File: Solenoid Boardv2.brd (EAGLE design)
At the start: 100 x 80 mm, 38 parts, among them Y2 ECS-80-S-4X

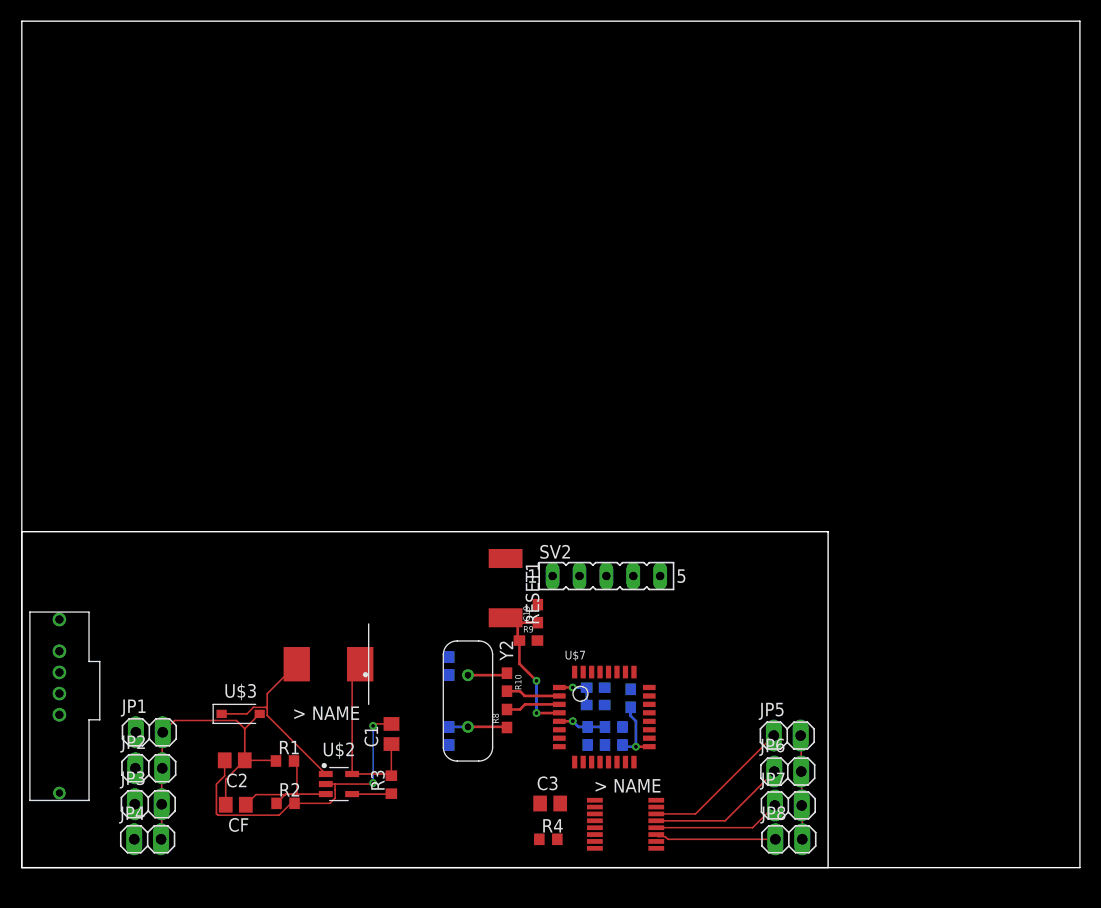
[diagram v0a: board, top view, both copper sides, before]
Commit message: Made progress on V2, added polygons and headers for step down converter
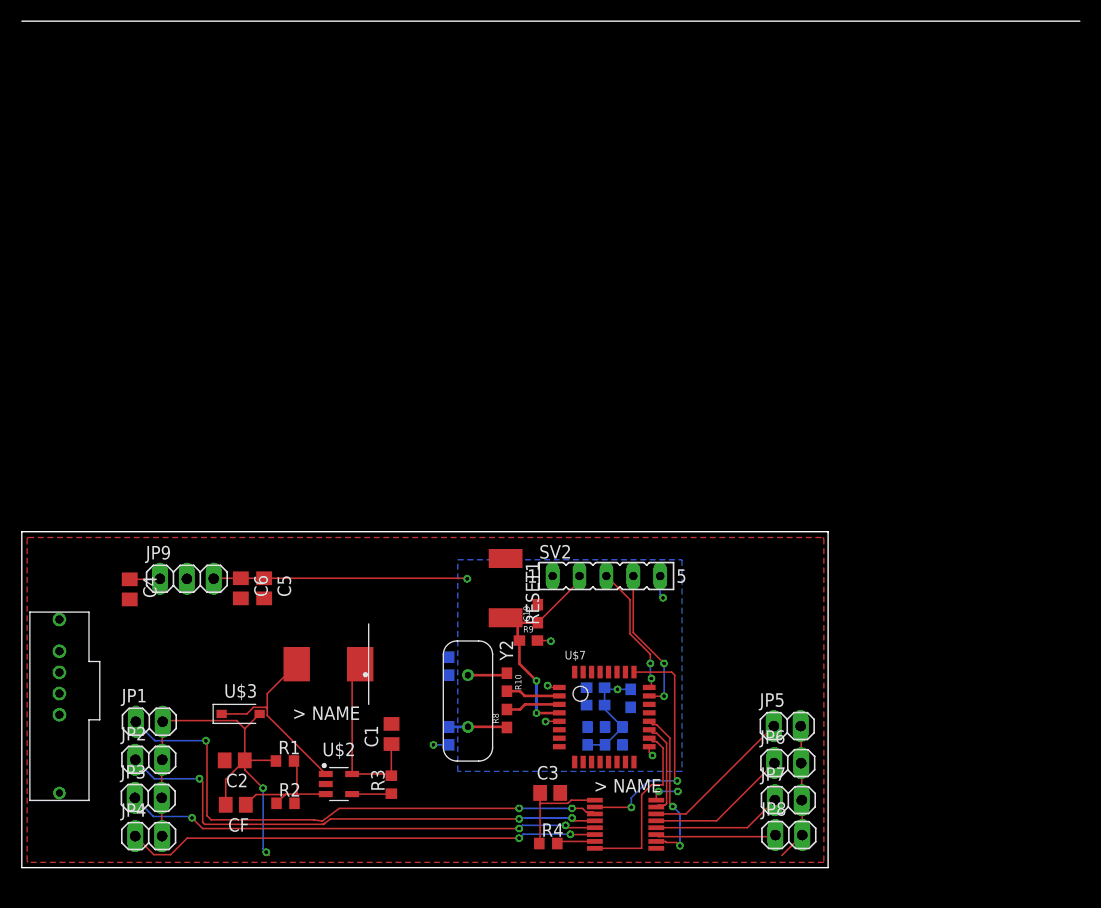
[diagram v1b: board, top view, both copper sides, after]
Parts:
- added C4: 10 µF, rcl:C0805
- added C5, C6: 47 µF, rcl:C0805
- added JP9: (no value), pinhead:1X03
- moved C3 1.00 mm to (49.9, 7.06)
- moved JP1 1.00 mm to (12.1, 13.8)
- moved JP5 0.90 mm to (72.3, 13.4)
- moved JP6 0.80 mm to (72.4, 9.88)
- moved JP2 0.80 mm to (12.0, 10.2)
- moved JP3 0.60 mm to (11.9, 6.59)
- moved JP7 0.50 mm to (72.4, 6.38)
- moved R4 0.40 mm to (49.8, 2.28)
- moved JP8 0.40 mm to (72.5, 3.08)
- moved JP4 0.32 mm to (12.0, 2.98)
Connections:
- net +12V: now also C4.1, JP9.1
- net +3V3: now also C5.1, C6.1, JP9.3
- net GND: now also C4.2, C5.2, C6.2, JP9.2
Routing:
- net DRAIN0: track 0.00 -> 51.9 mm, vias 0 -> 3
- net DRAIN1: track 0.00 -> 48.5 mm, vias 0 -> 3
- net DRAIN3: track 0.00 -> 45.0 mm, vias 0 -> 2
- net DRAIN2: track 0.00 -> 44.9 mm, vias 0 -> 3
- net SER_IN: track 0.00 -> 23.4 mm, vias 0 -> 2
- net G: track 0.00 -> 17.1 mm
- net +3V3: track 15.3 -> 30.9 mm, vias 3 -> 6
- net RCK: track 0.00 -> 15.6 mm, vias 0 -> 2
- net GND: track 30.4 -> 15.3 mm, vias 2 -> 4
- net SWDIO: track 0.00 -> 14.0 mm, vias 0 -> 2
- net +24V: track 41.5 -> 54.9 mm, vias 0 -> 2
- net SWCLK: track 0.00 -> 12.4 mm, vias 0 -> 2
- net +3.3V: track 0.00 -> 10.1 mm
- net SRCK: track 0.00 -> 8.99 mm
- net NRST: track 14.7 -> 20.7 mm
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- added copper zone on layer 16, net +3V3
- added copper zone on layer 1, net GND
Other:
- board size 100 x 80 mm -> 76.2 x 31.8 mm

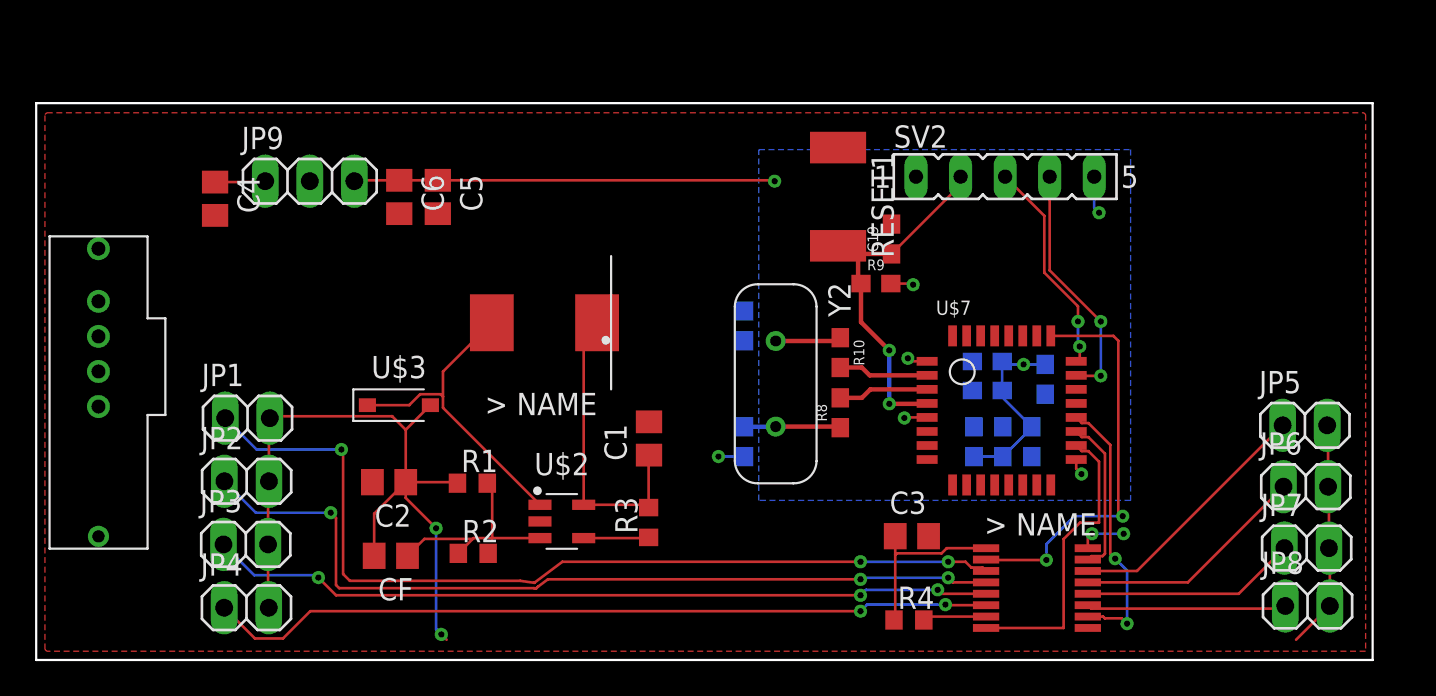
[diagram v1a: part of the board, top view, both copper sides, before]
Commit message: Added the can module
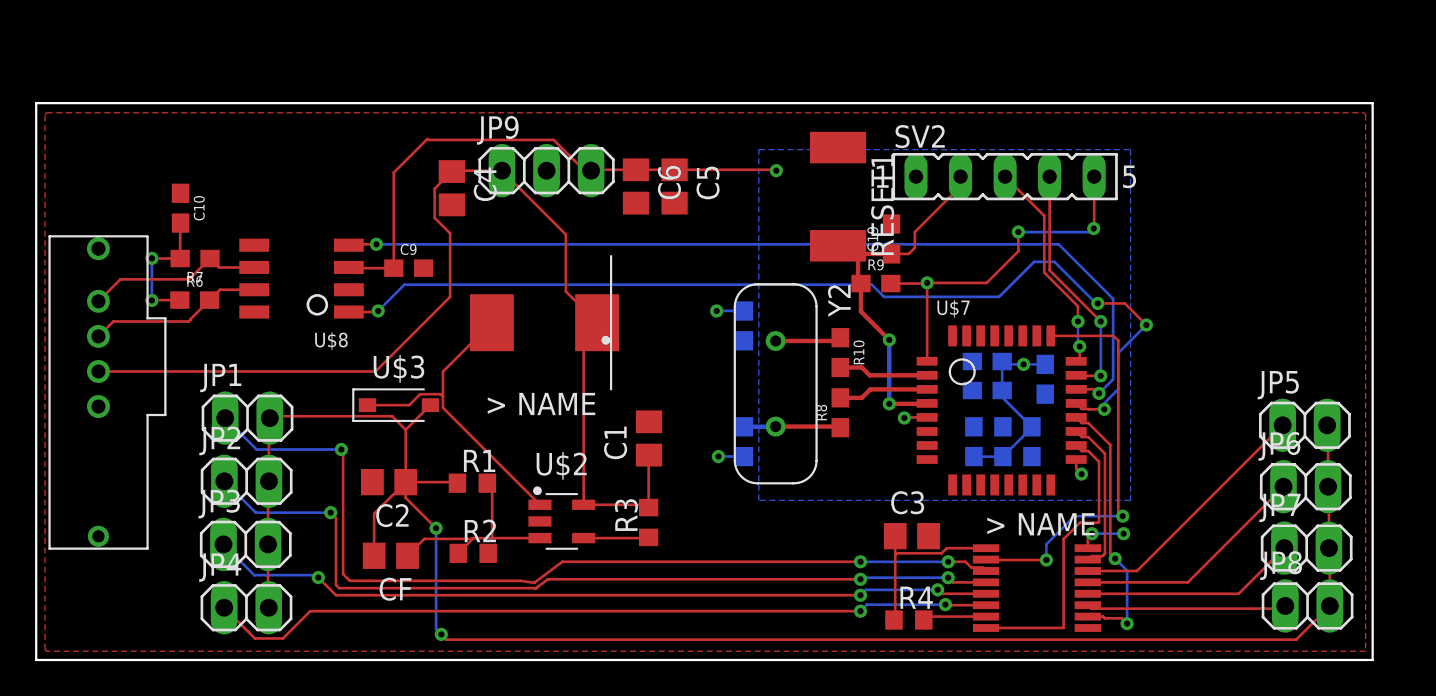
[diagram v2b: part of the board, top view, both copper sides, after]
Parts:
- added C10: 4.7nF, SparkFun-Capacitors:0603
- added C9: 100nF, SparkFun-Capacitors:0603
- added R6, R7: 60, SparkFun-Resistors:0603
- added U$8: TCAN337D, PI_Shield_Library:TCAN337D
- moved C6 13.5 mm to (34.2, 27.0)
- moved JP9 13.5 mm to (29.1, 27.9)
- moved C4 13.5 mm to (23.7, 26.9)
- moved C5 13.5 mm to (36.4, 27.0)
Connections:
- new net CAN_STM_RX: U$7.PA11, U$8.TXD
- new net CAN_STM_TX: U$7.PA12, U$8.RXD
- new net N$5: C10.2, R6.1, R7.2
- net +3V3: now also C9.1, U$8.VCC
- net CAN_H: now also R6.2, U$8.CANH
- net CAN_L: now also R7.1, U$8.CANL
- net GND: now also C10.1, C9.2, U$8.GND
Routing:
- net CAN_STM_RX: track 0.00 -> 56.3 mm, vias 0 -> 4
- net CAN_STM_TX: track 0.00 -> 52.0 mm, vias 0 -> 2
- net +24V: track 54.9 -> 103.4 mm
- net +12V: track 20.3 -> 61.9 mm
- net +3V3: track 30.9 -> 54.6 mm
- net CAN_L: track 0.00 -> 10.1 mm
- net CAN_H: track 0.00 -> 10.00 mm
- net N$5: track 0.00 -> 7.64 mm, vias 0 -> 2
- net GND: track 15.3 -> 16.9 mm, vias 4 -> 5
- net NRST: track 20.7 -> 21.5 mm

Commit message: changes from design review
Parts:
- added C7: 47uF, SparkFun-Capacitors:PANASONIC_D
- added H1, H2, H3: STAND-OFF, SparkFun-Hardware:STAND-OFF
- added U$4: 12-TO-3.3-DC-DC, minirov:MURATA-DCDC
- moved JP5 1.52 mm to (72.3, 11.9)
- moved JP6 1.27 mm to (72.4, 8.61)
- moved JP7 1.02 mm to (72.4, 5.36)
- moved JP8 1.02 mm to (72.5, 2.06)
- moved C3 0.51 mm to (49.9, 7.57)
- moved C14 0.25 mm to (57.0, 12.4)
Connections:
- net +12V: now also C7.+, U$4.VIN
- net +3V3: now also U$4.3.3V
- net GND: now also C7.-, U$4.GND
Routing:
- net +24V: track 103.4 -> 41.8 mm
- net +12V: track 61.9 -> 105.2 mm
- net +3V3: track 54.6 -> 88.2 mm, vias 6 -> 10
- net DRAIN6: track 12.3 -> 0.00 mm
- net DRAIN4: track 14.6 -> 2.80 mm
- net DRAIN7: track 11.4 -> 0.28 mm
- net DRAIN5: track 13.4 -> 5.71 mm
- net GND: track 16.9 -> 9.91 mm, vias 5 -> 8
- net RCK: track 15.6 -> 13.0 mm
- net SRCK: track 8.99 -> 6.82 mm
- net CAN_STM_RX: track 56.3 -> 57.5 mm
- net SWDIO: track 14.0 -> 12.9 mm
- net +3.3V: track 10.1 -> 10.7 mm
- added copper zone on layer 16, net GND
- removed copper zone on layer 16, net +3V3

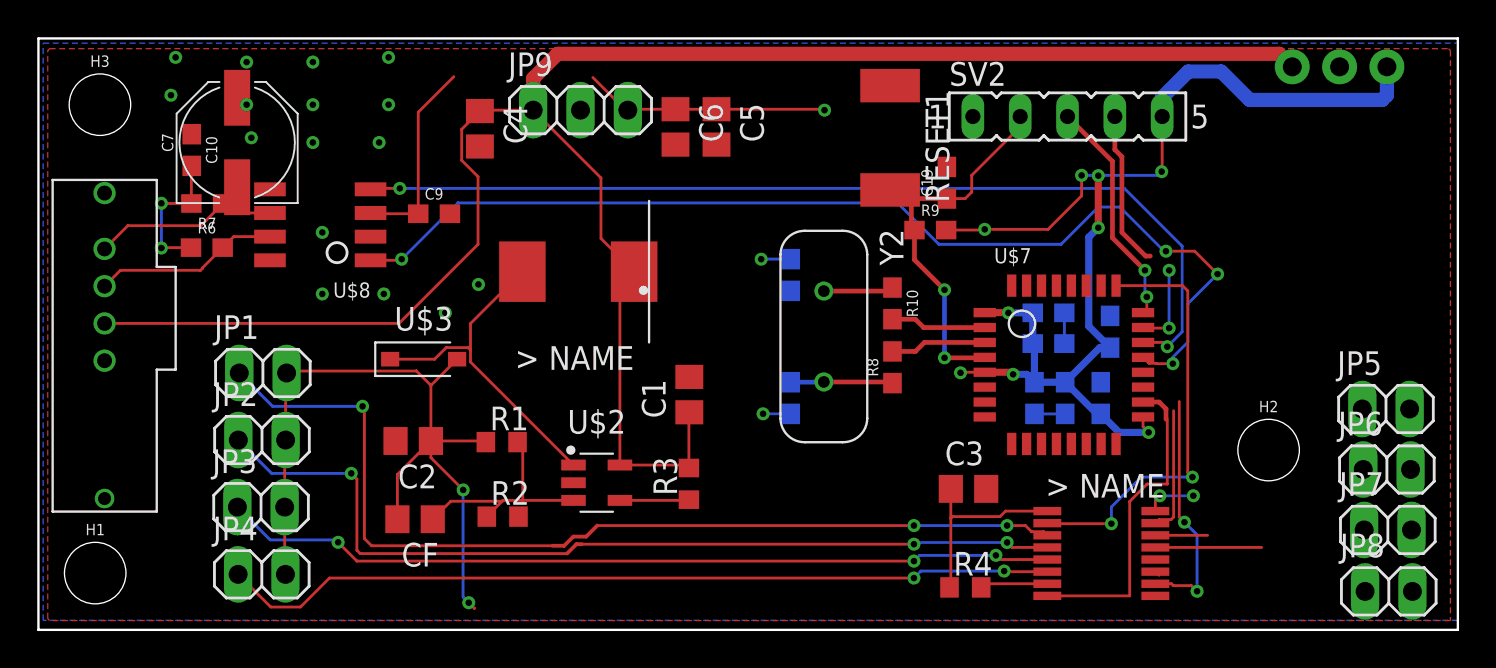
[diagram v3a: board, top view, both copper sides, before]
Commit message: WIP changing route widths
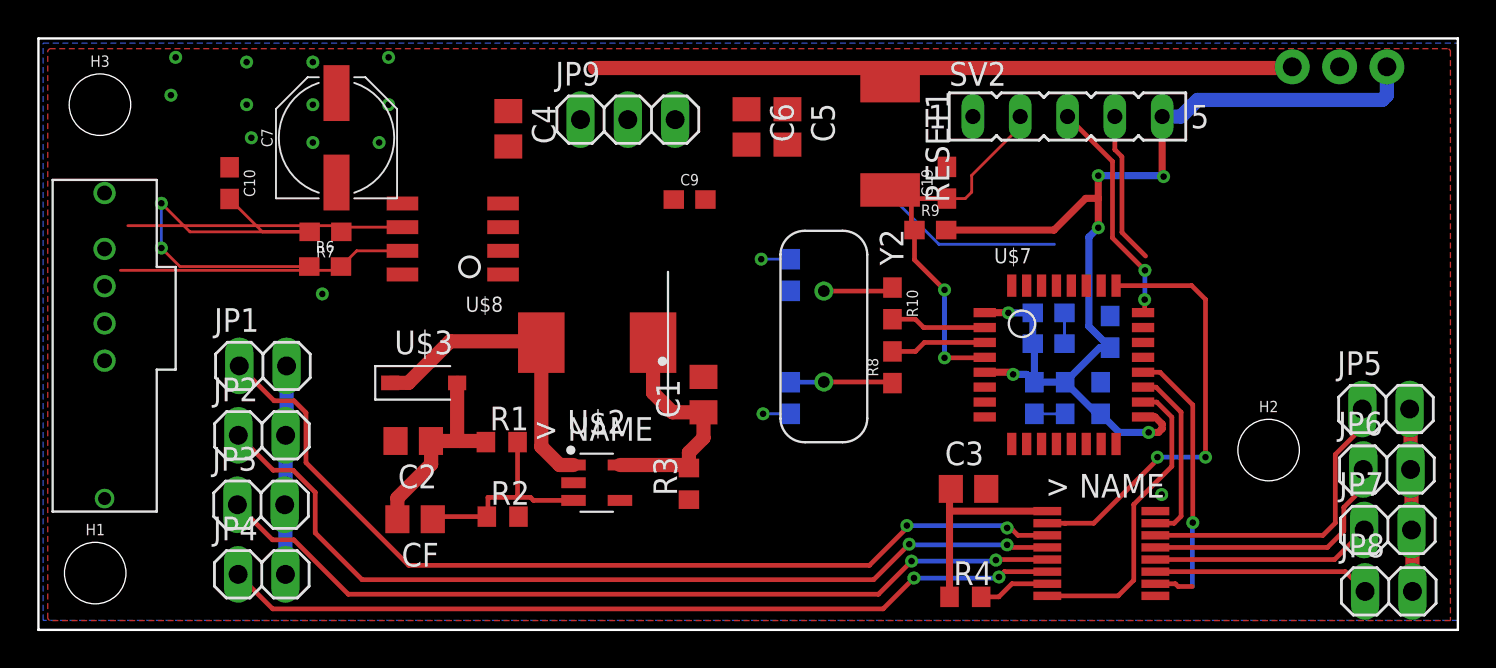
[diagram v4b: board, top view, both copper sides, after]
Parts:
- moved C9 13.7 mm to (35.0, 23.1)
- moved U$8 7.15 mm to (24.9, 22.9)
- moved R7 6.53 mm to (15.4, 21.4)
- moved R6 6.43 mm to (15.4, 19.5)
- moved C7 5.34 mm to (16.0, 26.4)
- moved I1 3.94 mm to (30.0, 15.4)
- moved C5 3.81 mm to (40.2, 27.0)
- moved C6 3.81 mm to (38.0, 27.0)
- moved C10 2.70 mm to (10.3, 24.0)
- moved JP9 2.59 mm to (31.6, 27.4)
- moved C4 1.52 mm to (25.2, 26.9)
- moved U$3 1.27 mm to (20.7, 13.3)
- moved C1 0.76 mm to (35.7, 12.6)
- moved R4 0.51 mm to (49.8, 1.77)
- moved JP1 0.38 mm to (12.1, 14.2)
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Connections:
- net +12V: now also U$5.4; no longer U$5.2
- net CAN_H: now also U$5.2; no longer U$5.3
- net CAN_L: now also U$5.3; no longer U$5.4
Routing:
- net +12V: track 105.2 -> 50.2 mm
- net CAN_STM_TX: track 52.0 -> 0.07 mm, vias 2 -> 0
- net CAN_STM_RX: track 57.5 -> 9.35 mm, vias 4 -> 0
- net +3V3: track 88.2 -> 61.6 mm, vias 10 -> 6
- net N$5: track 7.64 -> 24.4 mm
- net DRAIN4: track 2.80 -> 16.7 mm
- net DRAIN6: track 0.00 -> 11.9 mm
- net DRAIN7: track 0.28 -> 11.7 mm
- net +24V: track 41.8 -> 32.2 mm, vias 2 -> 0
- net DRAIN5: track 5.71 -> 14.2 mm
- net CAN_H: track 10.00 -> 15.6 mm
- net CAN_L: track 10.1 -> 15.0 mm
- net SWDIO: track 12.9 -> 8.22 mm, vias 2 -> 0
- net SHDN: track 3.72 -> 0.06 mm
- net SRCK: track 6.82 -> 9.72 mm
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
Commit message: Added required revisions from design review
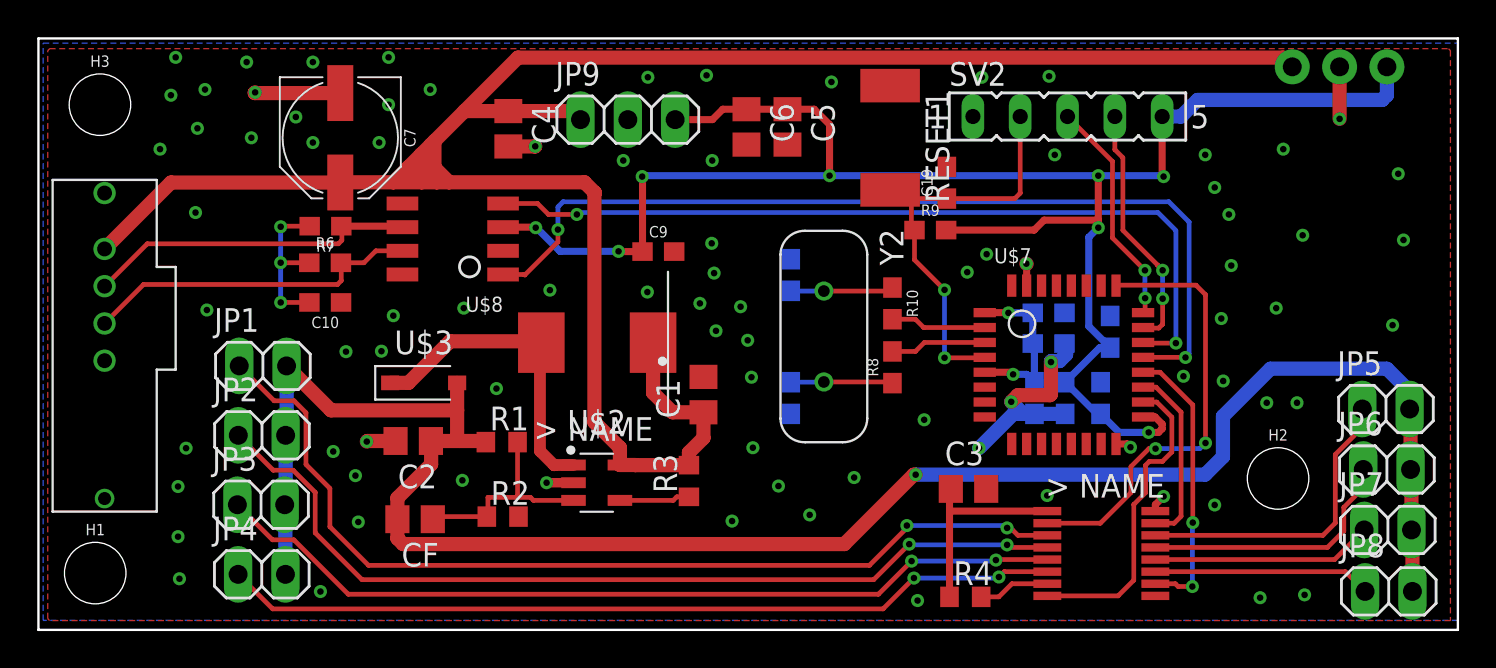
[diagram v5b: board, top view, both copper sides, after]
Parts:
- moved C10 8.21 mm to (15.4, 17.6), turned to 180 degrees
- moved C9 3.26 mm to (33.3, 20.3)
- moved H2 1.61 mm to (66.5, 8.13)
- moved R7 0.30 mm to (15.4, 21.7)
- moved C7 0.20 mm to (16.2, 26.4), turned to 270 degrees
- moved R6 0.20 mm to (15.4, 19.7)
- moved R3 0.15 mm to (34.9, 7.99)
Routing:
- net +24V: track 32.2 -> 104.5 mm, vias 0 -> 1
- net +12V: track 50.2 -> 121.1 mm
- net +3V3: track 61.6 -> 109.2 mm, vias 6 -> 10
- net CAN_STM_TX: track 0.07 -> 44.6 mm, vias 0 -> 2
- net CAN_STM_RX: track 9.35 -> 49.7 mm, vias 0 -> 2
- net GND: track 7.04 -> 27.5 mm, vias 5 -> 13
- net N$5: track 24.4 -> 8.71 mm, vias 2 -> 3
- net SWDIO: track 8.22 -> 13.4 mm, vias 0 -> 2
- net SHDN: track 0.06 -> 3.78 mm
- net CAN_L: track 15.0 -> 17.8 mm
- net CAN_H: track 15.6 -> 18.2 mm
- net N$4: track 3.76 -> 5.54 mm
- net NRST: track 21.5 -> 22.9 mm
- net DRAIN0: track 50.6 -> 51.8 mm
- net RCK: vias 1 -> 2
